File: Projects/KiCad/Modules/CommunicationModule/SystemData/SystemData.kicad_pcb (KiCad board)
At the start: 2 copper layers, 110 x 95 mm, 39 parts, among them J1 Conn_01x08, SW1 SW_DIP_x02, U1 MCP2562-E-P, U2 MCP2515-I/P, U3 NJM7805SDL1, U4 ABX00012, Y1 8MHz

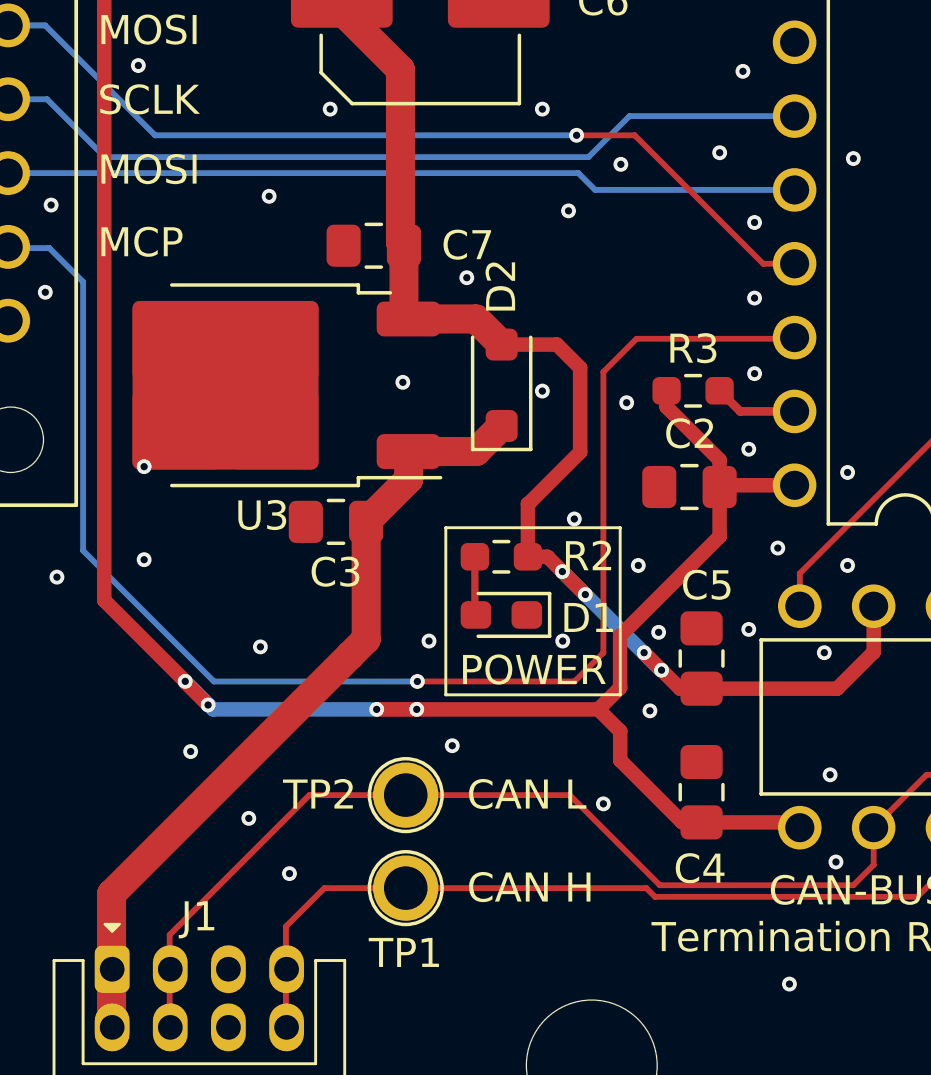
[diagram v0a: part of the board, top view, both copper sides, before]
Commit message: チップ積層セラミックコンデンサをSMD1608に変更
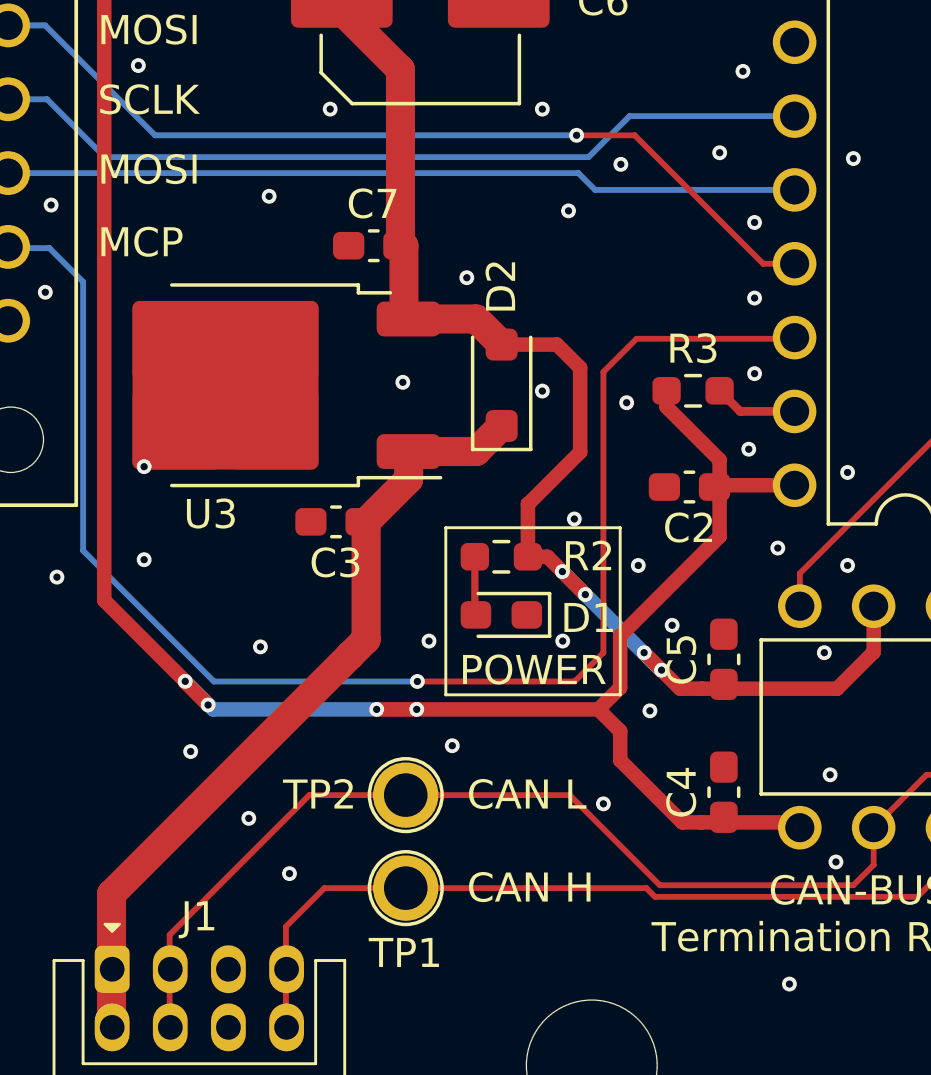
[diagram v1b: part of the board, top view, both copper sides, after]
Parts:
- C2, C4, C5, C7: footprint Capacitor_SMD:C_0805_2012Metric_Pad1.18x1.45mm_HandSolder -> Capacitor_SMD:C_0603_1608Metric_Pad1.08x0.95mm_HandSolder
- C3: value 0.33μF -> 10μF; footprint Capacitor_SMD:C_0805_2012Metric_Pad1.18x1.45mm_HandSolder -> Capacitor_SMD:C_0603_1608Metric_Pad1.08x0.95mm_HandSolder
- moved C5 0.77 mm to (183.0, 121.0)
- moved C4 0.77 mm to (183.0, 125.6)
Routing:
- net GND: vias 150 -> 149

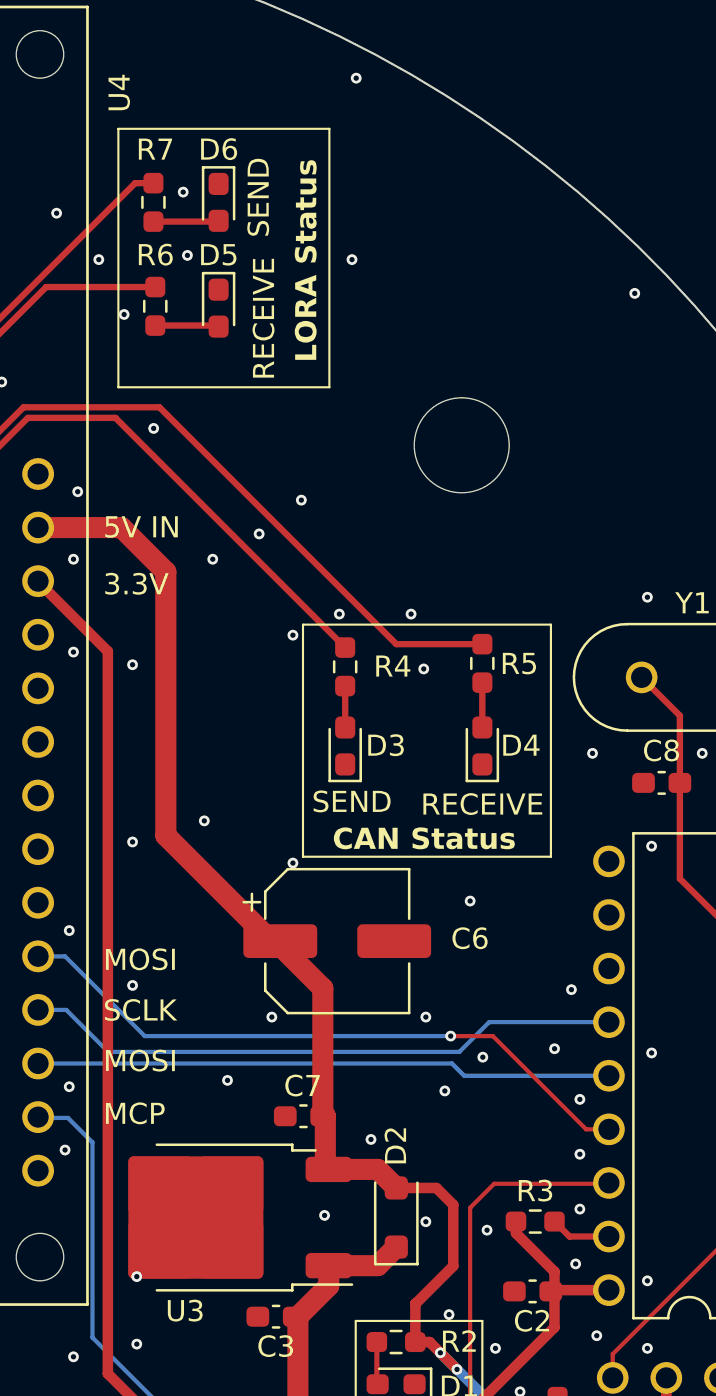
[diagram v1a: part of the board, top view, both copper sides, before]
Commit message: 抵抗の在庫に合わせてサイズを変更
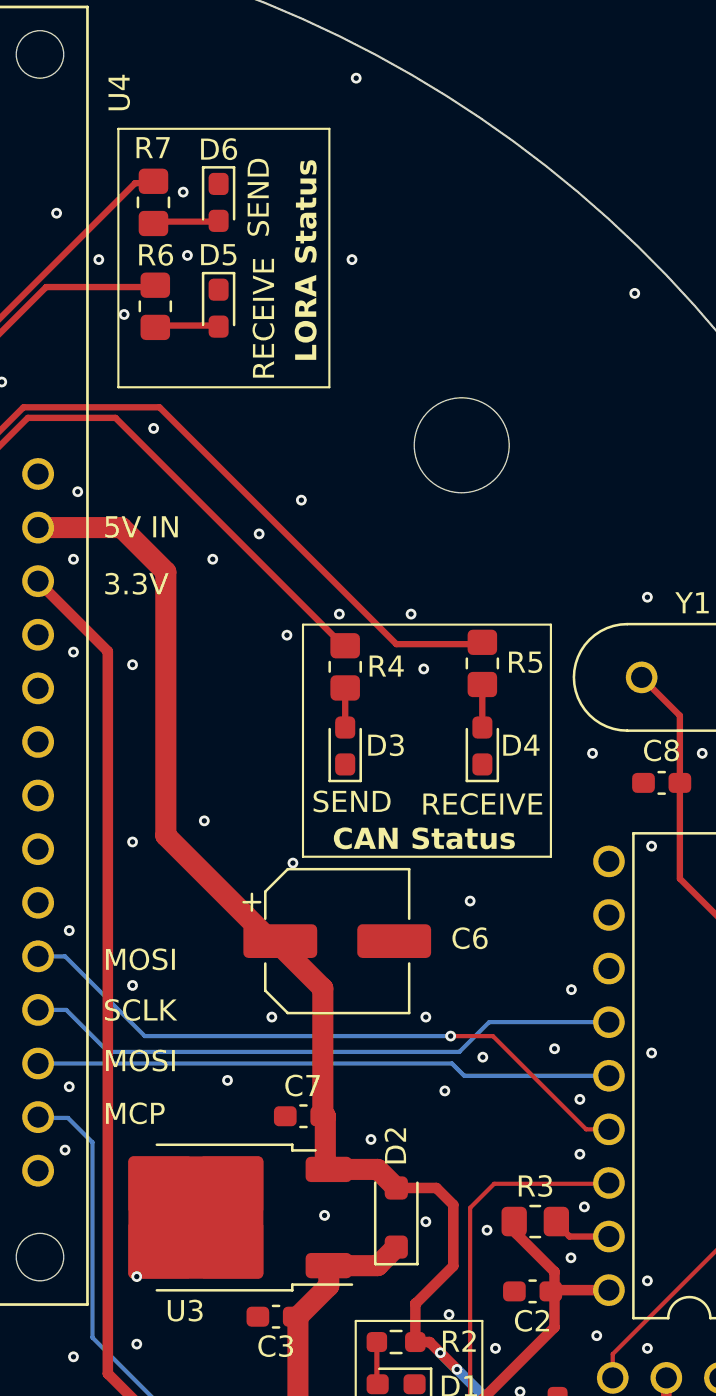
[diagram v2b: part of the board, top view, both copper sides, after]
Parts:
- R3, R4, R5, R6, R7: footprint Resistor_SMD:R_0603_1608Metric_Pad0.98x0.95mm_HandSolder -> Resistor_SMD:R_0805_2012Metric_Pad1.20x1.40mm_HandSolder

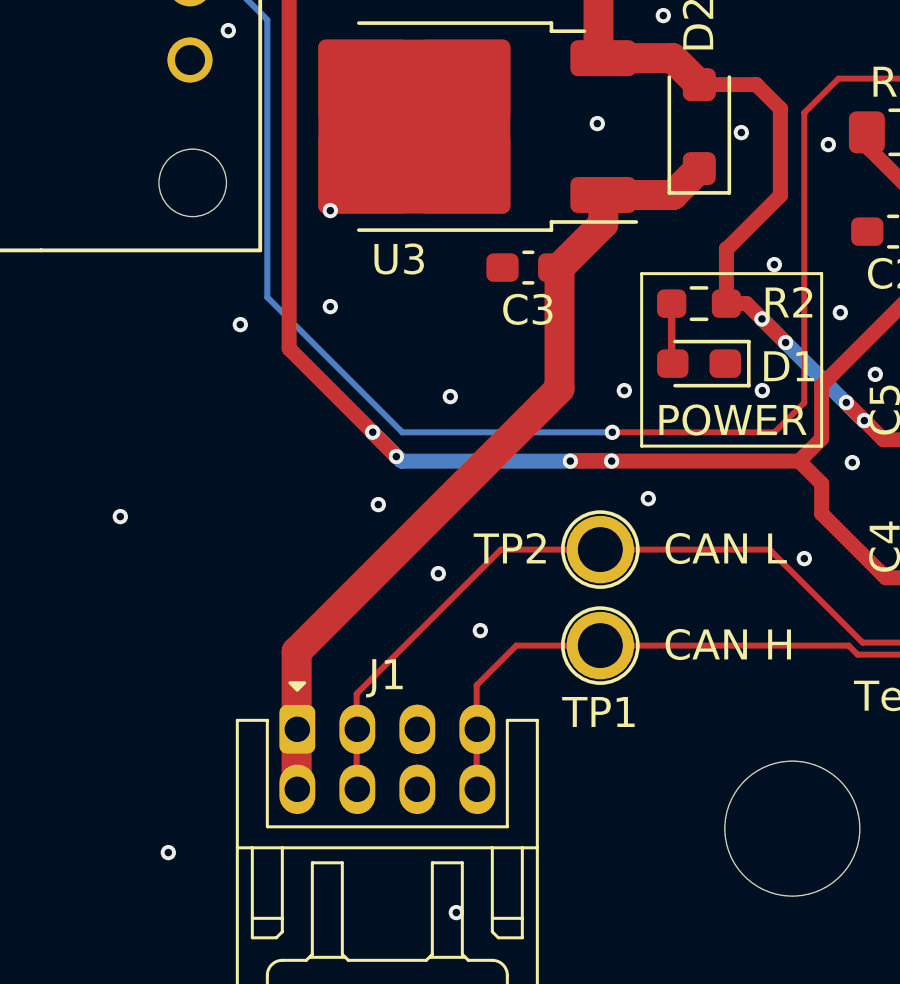
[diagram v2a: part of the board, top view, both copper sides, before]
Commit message: コネクタ位置を揃えた
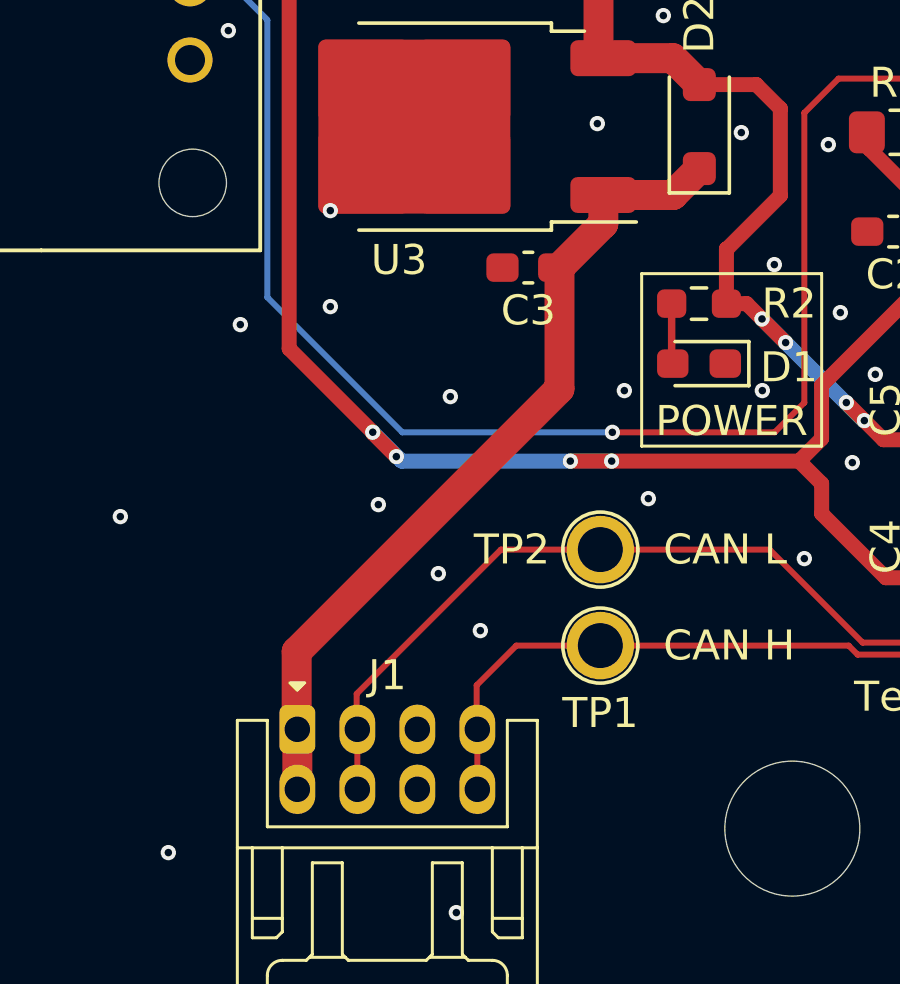
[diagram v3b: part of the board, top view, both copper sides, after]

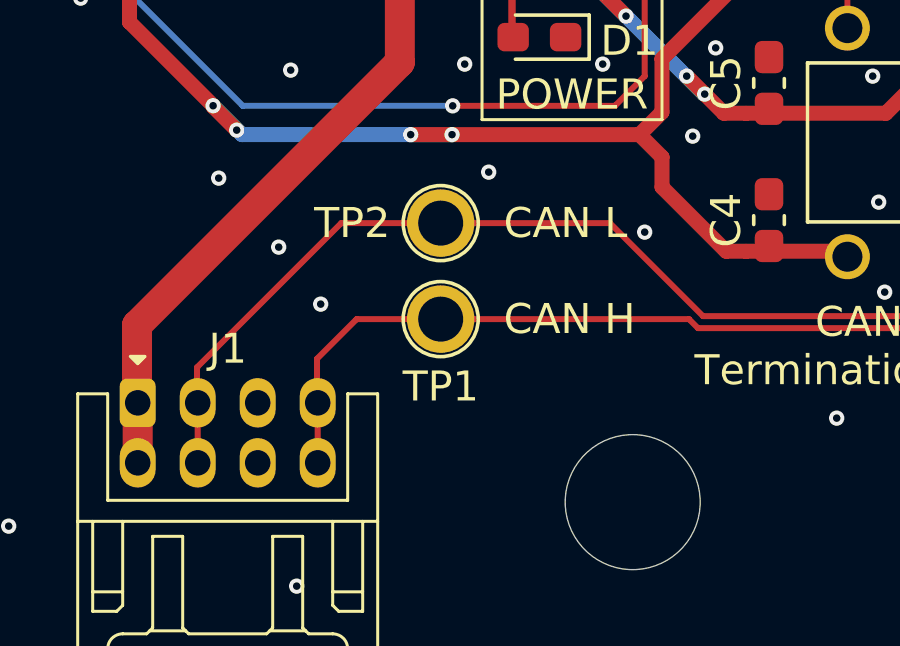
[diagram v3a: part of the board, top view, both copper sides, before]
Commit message: コネクタのピン配置を変更
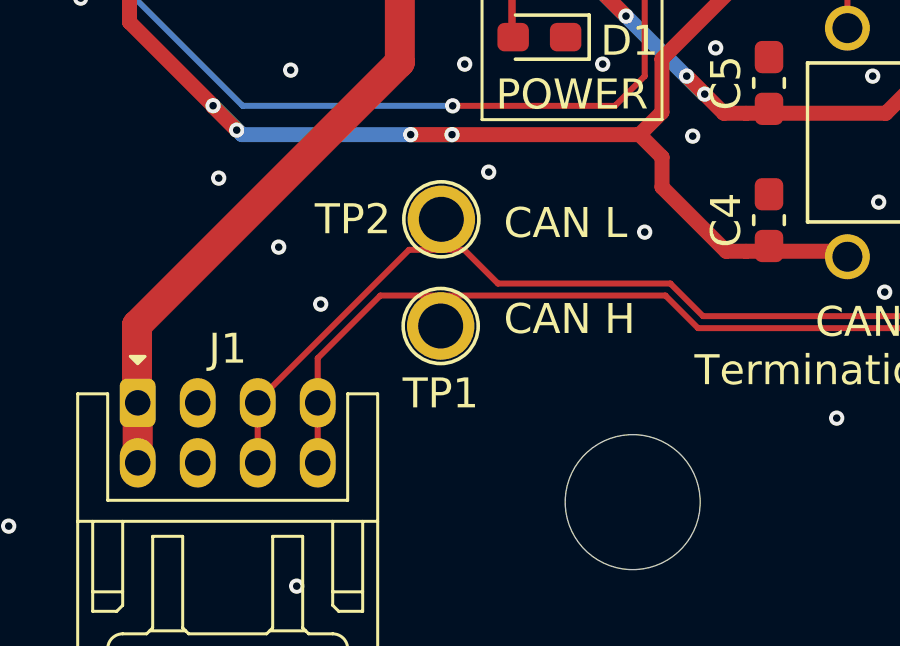
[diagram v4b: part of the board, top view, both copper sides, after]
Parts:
- moved TP1 0.23 mm to (172.1, 129.1)
- moved TP2 0.13 mm to (172.1, 125.6)
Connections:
- J1 pad 3: CAN_L -> GND
- J1 pad 4: CAN_L -> GND
- J1 pad 5: GND -> CAN_L
- J1 pad 6: GND -> CAN_L
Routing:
- net CAN_L: track 44.4 -> 41.0 mm
- net CAN_H: track 38.6 -> 39.2 mm

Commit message: クリスタルをSMDに変更
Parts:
- Y1: footprint Crystal:Crystal_HC49-U_Vertical -> Crystal:Crystal_SMD_HC49-SD
- moved C1 6.21 mm to (195.2, 85.7)
- moved C8 6.06 mm to (185.0, 85.7)
- moved Y1 4.87 mm to (190.1, 89.8)
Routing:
- net OSC2: track 16.3 -> 19.3 mm
- net OSC1: track 12.4 -> 14.6 mm
- net GND: vias 149 -> 146

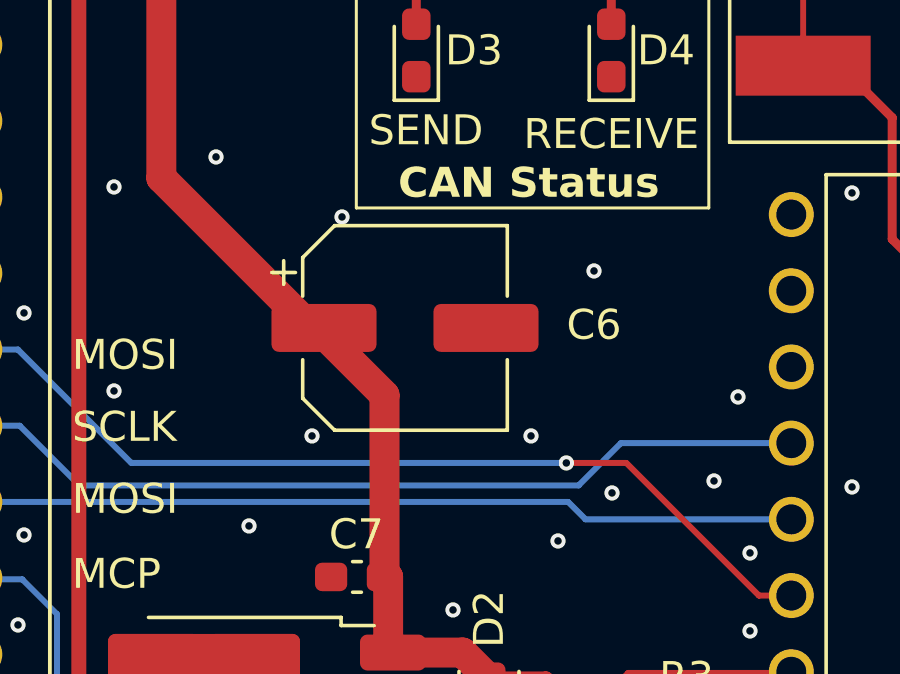
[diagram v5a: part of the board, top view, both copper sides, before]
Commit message: バッファコンデンサを表面実装に変更
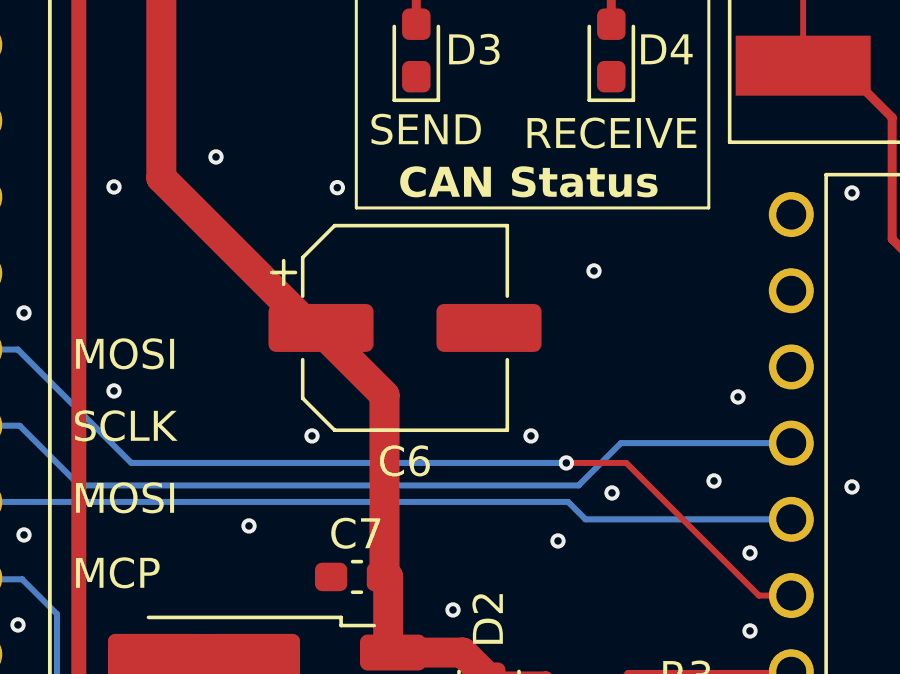
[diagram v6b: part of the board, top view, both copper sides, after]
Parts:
- C6: value 100μF -> 47μF; footprint Capacitor_SMD:CP_Elec_6.3x7.7 -> Capacitor_SMD:CP_Elec_6.3x5.9

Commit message: チェックよし（多分）
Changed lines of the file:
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@@
     (fp_line (start 1 0.625) (end -1 0.625)
       (stroke (width 0.1) (type solid)) (layer "F.Fab"))
-    (pad "1" smd roundrect (at -1 0 270) (size 1.2 1.4) (layers "F.Cu" "F.Paste" "F.Mask") (roundrect_rratio 0.208333)
+    (pad "1" smd roundrect (at -1 0 270) (size 1.2 1.4) (layers "F.Cu" "F.Paste" "F.Mask") (roundrect_rratio 0.2083333333)
       (net 71 "LORA_RECEIVE_STATUS") (pintype "passive"))
-    (pad "2" smd roundrect (at 1 0 270) (size 1.2 1.4) (layers "F.Cu" "F.Paste" "F.Mask") (roundrect_rratio 0.208333)
+    (pad "2" smd roundrect (at 1 0 270) (size 1.2 1.4) (layers "F.Cu" "F.Paste" "F.Mask") (roundrect_rratio 0.2083333333)
       (net 67 "Net-(D5-A)") (pintype "passive"))
     (model "${KICAD6_3DMODEL_DIR}/Resistor_SMD.3dshapes/R_0805_2012Metric.wrl"
@@
     (fp_line (start 1 0.625) (end -1 0.625)
       (stroke (width 0.1) (type solid)) (layer "F.Fab"))
-    (pad "1" smd roundrect (at -1 0 270) (size 1.2 1.4) (layers "F.Cu" "F.Paste" "F.Mask") (roundrect_rratio 0.208333)
+    (pad "1" smd roundrect (at -1 0 270) (size 1.2 1.4) (layers "F.Cu" "F.Paste" "F.Mask") (roundrect_rratio 0.2083333333)
       (net 70 "CAN_SEND_STATUS") (pintype "passive"))
-    (pad "2" smd roundrect (at 1 0 270) (size 1.2 1.4) (layers "F.Cu" "F.Paste" "F.Mask") (roundrect_rratio 0.208333)
+    (pad "2" smd roundrect (at 1 0 270) (size 1.2 1.4) (layers "F.Cu" "F.Paste" "F.Mask") (roundrect_rratio 0.2083333333)
       (net 65 "Net-(D3-A)") (pintype "passive"))
     (model "${KICAD6_3DMODEL_DIR}/Resistor_SMD.3dshapes/R_0805_2012Metric.wrl"
@@
     (fp_line (start 1 0.625) (end -1 0.625)
       (stroke (width 0.1) (type solid)) (layer "F.Fab"))
-    (pad "1" smd roundrect (at -1 0) (size 1.2 1.4) (layers "F.Cu" "F.Paste" "F.Mask") (roundrect_rratio 0.208333)
+    (pad "1" smd roundrect (at -1 0) (size 1.2 1.4) (layers "F.Cu" "F.Paste" "F.Mask") (roundrect_rratio 0.2083333333)
       (net 5 "+3.3V") (pintype "passive"))
-    (pad "2" smd roundrect (at 1 0) (size 1.2 1.4) (layers "F.Cu" "F.Paste" "F.Mask") (roundrect_rratio 0.208333)
+    (pad "2" smd roundrect (at 1 0) (size 1.2 1.4) (layers "F.Cu" "F.Paste" "F.Mask") (roundrect_rratio 0.2083333333)
       (net 15 "Net-(U2-~RESET)") (pintype "passive"))
     (model "${KICAD6_3DMODEL_DIR}/Resistor_SMD.3dshapes/R_0805_2012Metric.wrl"
@@
     (fp_line (start 1 0.625) (end -1 0.625)
       (stroke (width 0.1) (type solid)) (layer "F.Fab"))
-    (pad "1" smd roundrect (at -1 0 270) (size 1.2 1.4) (layers "F.Cu" "F.Paste" "F.Mask") (roundrect_rratio 0.208333)
+    (pad "1" smd roundrect (at -1 0 270) (size 1.2 1.4) (layers "F.Cu" "F.Paste" "F.Mask") (roundrect_rratio 0.2083333333)
       (net 72 "LORA_SEND_STATUS") (pintype "passive"))
-    (pad "2" smd roundrect (at 1 0 270) (size 1.2 1.4) (layers "F.Cu" "F.Paste" "F.Mask") (roundrect_rratio 0.208333)
+    (pad "2" smd roundrect (at 1 0 270) (size 1.2 1.4) (layers "F.Cu" "F.Paste" "F.Mask") (roundrect_rratio 0.2083333333)
       (net 68 "Net-(D6-A)") (pintype "passive"))
     (model "${KICAD6_3DMODEL_DIR}/Resistor_SMD.3dshapes/R_0805_2012Metric.wrl"
@@
     (fp_line (start 1 0.625) (end -1 0.625)
       (stroke (width 0.1) (type solid)) (layer "F.Fab"))
-    (pad "1" smd roundrect (at -1 0 270) (size 1.2 1.4) (layers "F.Cu" "F.Paste" "F.Mask") (roundrect_rratio 0.208333)
+    (pad "1" smd roundrect (at -1 0 270) (size 1.2 1.4) (layers "F.Cu" "F.Paste" "F.Mask") (roundrect_rratio 0.2083333333)
       (net 69 "CAN_RECEIVE_STATUS") (pintype "passive"))
-    (pad "2" smd roundrect (at 1 0 270) (size 1.2 1.4) (layers "F.Cu" "F.Paste" "F.Mask") (roundrect_rratio 0.208333)
+    (pad "2" smd roundrect (at 1 0 270) (size 1.2 1.4) (layers "F.Cu" "F.Paste" "F.Mask") (roundrect_rratio 0.2083333333)
       (net 66 "Net-(D4-A)") (pintype "passive"))
     (model "${KICAD6_3DMODEL_DIR}/Resistor_SMD.3dshapes/R_0805_2012Metric.wrl"

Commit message: 配線の繋ぎ忘れを修正
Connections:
- U4 pad 25: unconnected-(U4-GND-Pad25) -> GND
